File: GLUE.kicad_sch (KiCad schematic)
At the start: 7 parts, among them J3 AVR-JTAG-10, U18 ATF1508-100

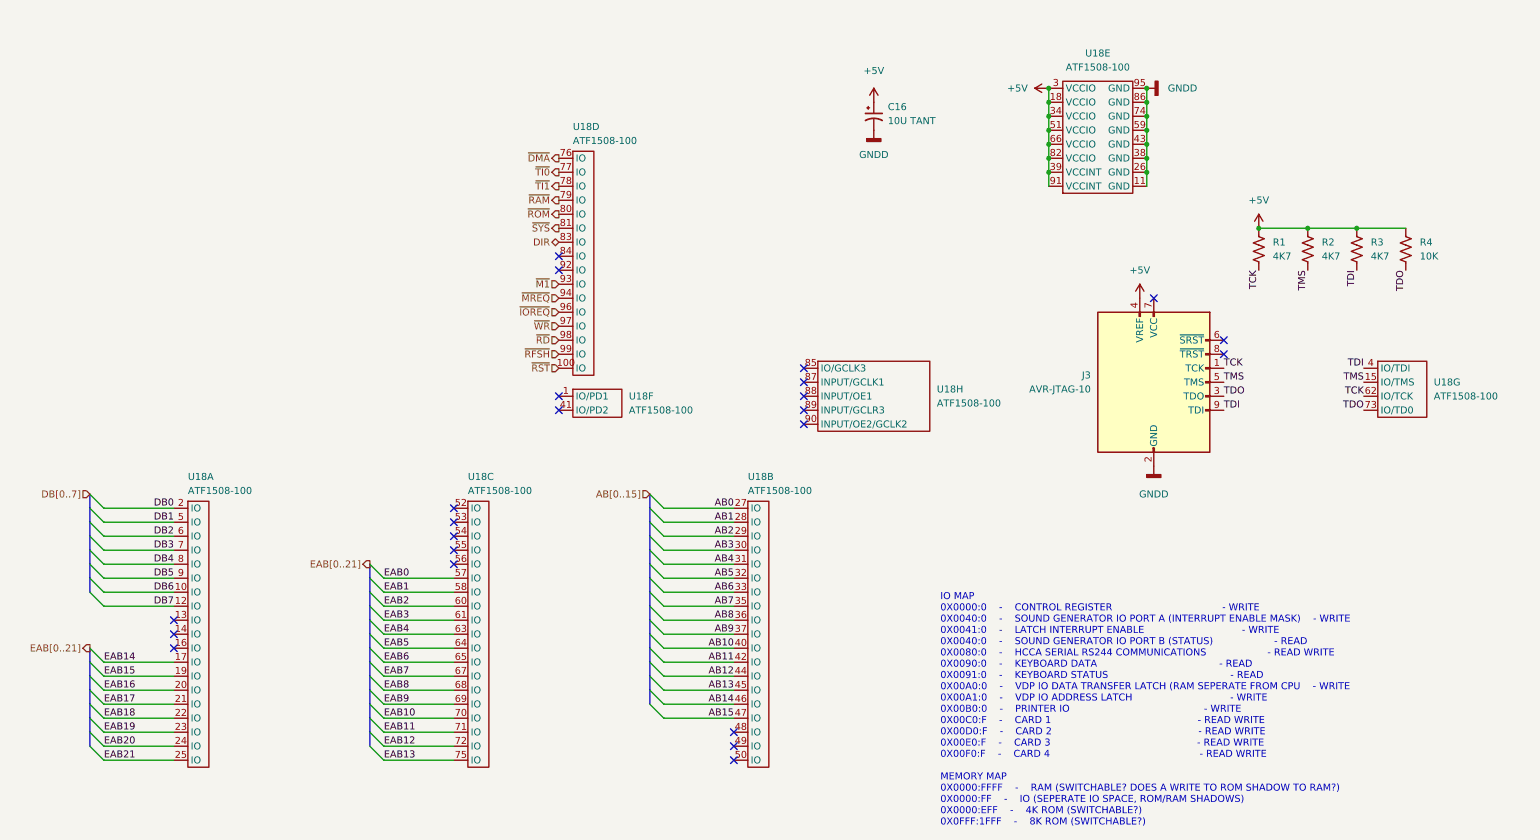
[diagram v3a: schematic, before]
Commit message: simplified the vhdl code for the mapper by removing some of the more complex initilization logic used:     flags was initially intended to be used for reset logic but     was determined to be un-needed if we initialise as done in     the generate loop for the bank registers
    control_regs was going to shadow the main system control
    register, but only contain the bits not used by the system.
    removed for now since im not sure that those bits arent
    written anyway by software. the eventual intention is to
    allow bits 7 and 8 to determine if mapping is wanted at all
    and to boot from interposer rom instead of network (which may
    end up being done anyway if i can figure out how)

    other logical simplfications where also performed such as
    removing the need for plumbing the address bus through the
    glue logic at all. this is reflected in the schematics

    the interposer glue logic now only needs 8 address lines
    to swing the extended address bus around.
the schematics where simplified so that the entire address bus
isnt routed through the interposer now. may end up using a
smaller 1508 beucase of this.

a liscense file was added to the vhd file(s) and the mapper file
was broken up into a package and main buildable, the beginings of
a test bench was added, now begins the slog of verification!
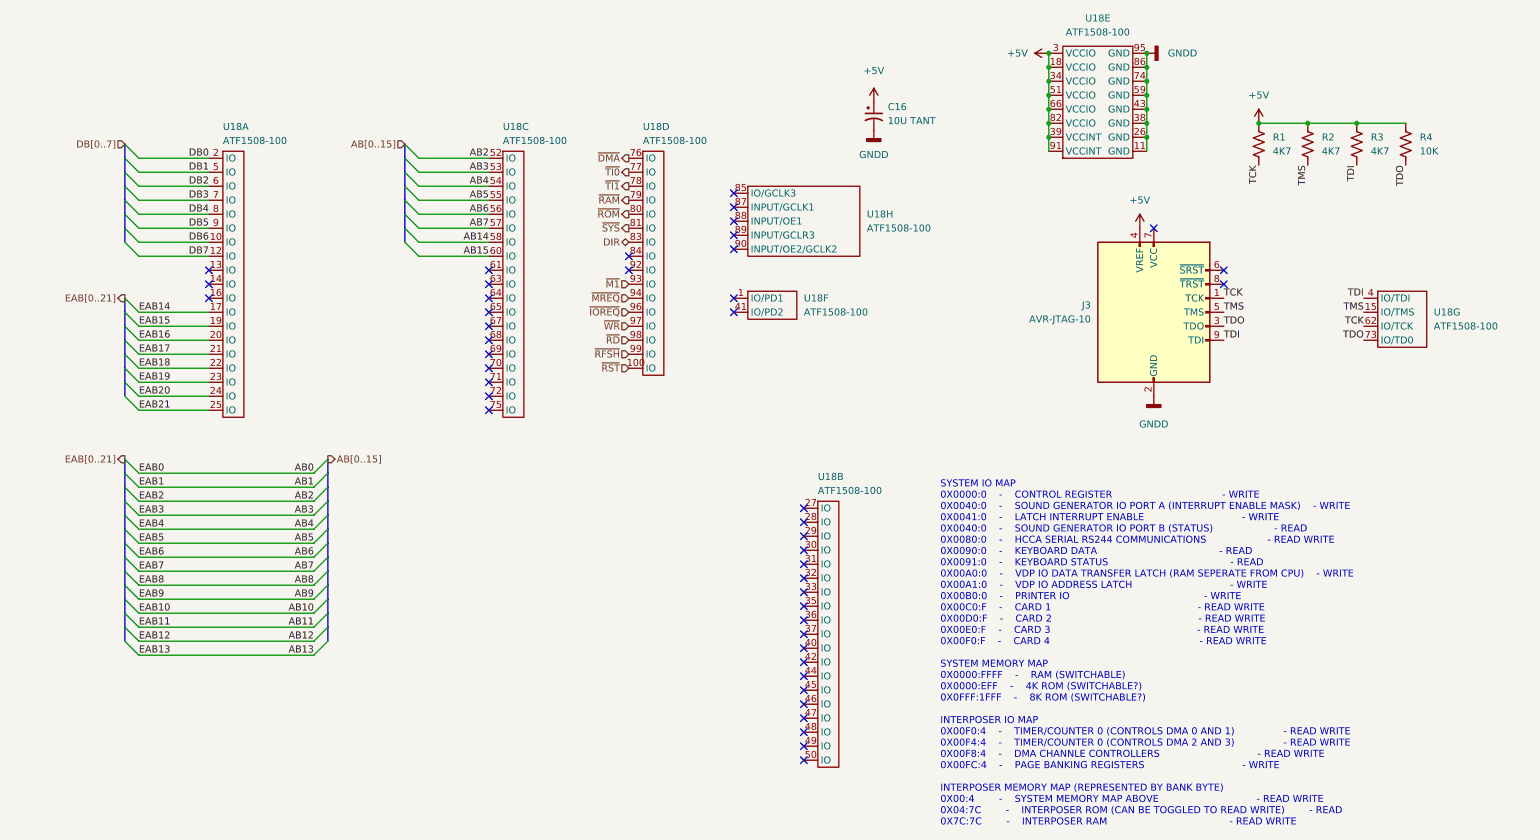
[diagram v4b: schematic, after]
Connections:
- net EAB0 is gone; now on net AB7: U18.57 (IO)
- net EAB1 is gone; now on net AB14: U18.58 (IO)
- net EAB2 is gone; now on net AB15: U18.60 (IO)
- net AB0: no longer U18.27 (IO)
- net AB1: no longer U18.28 (IO)
- net AB10: no longer U18.40 (IO)
- net AB11: no longer U18.42 (IO)
- net AB12: no longer U18.44 (IO)
- net AB13: no longer U18.45 (IO)
- net AB14: no longer U18.46 (IO)
- net AB15: no longer U18.47 (IO)
- net AB2: now also U18.52 (IO); no longer U18.29 (IO)
- net AB3: now also U18.53 (IO); no longer U18.30 (IO)
- net AB4: now also U18.54 (IO); no longer U18.31 (IO)
- net AB5: now also U18.55 (IO); no longer U18.32 (IO)
- net AB6: now also U18.56 (IO); no longer U18.33 (IO)
- net AB7: no longer U18.35 (IO)
- net AB8: no longer U18.36 (IO)
- net AB9: no longer U18.37 (IO)
- net EAB10: no longer names the net of U18.70 (IO)
- net EAB11: no longer names the net of U18.71 (IO)
- net EAB12: no longer names the net of U18.72 (IO)
- net EAB13: no longer names the net of U18.75 (IO)
- net EAB3: no longer names the net of U18.61 (IO)
- net EAB4: no longer names the net of U18.63 (IO)
- net EAB5: no longer names the net of U18.64 (IO)
- net EAB6: no longer names the net of U18.65 (IO)
- net EAB7: no longer names the net of U18.67 (IO)
- net EAB8: no longer names the net of U18.68 (IO)
- net EAB9: no longer names the net of U18.69 (IO)
- no-connect marks 23 -> 45
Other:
- note added: "SYSTEM IO MAP 0X0000:0 - CONTROL REGISTER - WRITE 0X0040:0 - SOUND GENERATOR IO PORT A (INTERRUPT ENABLE MASK) - WRITE 0X0041:0 - LATCH INTERRUPT ENABLE - WRITE 0X0040:0 - SOUND GENERATOR IO PORT B (STATUS) - READ 0X0080:0 - HCCA SERIAL RS244 COMMUNICATIONS - READ WRITE 0X0090:0 - KEYBOARD DATA - READ 0X0091:0 - KEYBOARD STATUS - READ 0X00A0:0 - VDP IO DATA TRANSFER LATCH (RAM SEPERATE FROM CPU) 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"
- note removed: "IO MAP 0X0000:0 - CONTROL REGISTER - WRITE 0X0040:0 - SOUND GENERATOR IO PORT A (INTERRUPT ENABLE MASK) - WRITE 0X0041:0 - LATCH INTERRUPT ENABLE - WRITE 0X0040:0 - SOUND GENERATOR IO PORT B (STATUS) - READ 0X0080:0 - HCCA SERIAL RS244 COMMUNICATIONS - READ WRITE 0X0090:0 - KEYBOARD DATA - READ 0X0091:0 - KEYBOARD STATUS - READ 0X00A0:0 - VDP IO DATA TRANSFER LATCH (RAM SEPERATE FROM CPU - WRITE 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"
- moved on the sheet: J3, R1, R2, R3, R4, U18A, U18B, U18C, U18D, U18E, U18F, U18G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

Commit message: final hardware revision
final update to the hardware:
- removed flash
- added battery backup switch-over
- increased ram to 4MB
- added ramboot/netboot option by using reads to write-only ports to trigger/toggle
- fixed a logic bug i should have caught in writes to the mapper registers (using bits 14&15 instead of 1&0)
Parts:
- added U11: 74LVC2G74, Package_TO_SOT_SMD:SOT-363_SC-70-6, symbol 74xGxx:74LVC2G74
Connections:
- net ~{ROM} is gone; now on net ~{SYS}: U18.80 (IO)
- net AB0: now also U18.52 (IO)
- net AB1: now also U18.53 (IO)
- net AB14: now also U18.61 (IO); no longer U18.58 (IO)
- net AB15: now also U18.63 (IO); no longer U18.60 (IO)
- net AB2: now also U18.54 (IO); no longer U18.52 (IO)
- net AB3: now also U18.55 (IO); no longer U18.53 (IO)
- net AB4: now also U18.56 (IO); no longer U18.54 (IO)
- net AB5: now also U18.57 (IO); no longer U18.55 (IO)
- net AB6: now also U18.58 (IO); no longer U18.56 (IO)
- net AB7: now also U18.60 (IO); no longer U18.57 (IO)
- net DIR: now also U18.81 (IO); no longer U18.83 (IO)
- net ~{SYS}: no longer U18.81 (IO)
- net ~{RAMBOOT}: now reaches U18.84 (IO)
- net ~{RAMBOOT}: now also U11.6 (~{CLR})
- net BOOTTYPE: now reaches U18.92 (IO)
- net BOOTTYPE: now also U11.5 (Q)
- net GNDD renamed GND
- net GND: now also U11.1 (C), U11.2 (D), U11.4 (GND)
- new net +3V3: U11.8 (VCC)
- new net ~{NETBOOT}: U11.7 (~{PRE}), U18.83 (IO)
- no-connect marks 45 -> 42
